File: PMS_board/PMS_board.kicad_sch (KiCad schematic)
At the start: 0 parts

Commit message: Added a Battery Managment chip
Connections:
- no-connect marks 0 -> 15
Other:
- added sheet Battery Management (BatteryManagement.kicad_sch)
- note added: "Temporarily put no connects to make ERC shut up"
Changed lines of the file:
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@@
 	(generator_version "10.0")
 	(paper "A4")
+	(text "Temporarily put no connects \nto make ERC shut up"
+		(exclude_from_sim no)
+		(at 88.646 48.006 0)
+		(effects
+			(font
+				(size 1.27 1.27)
+			)
+		)
+	)
+	(no_connect
+		(at 40.64 59.69)
+	)
+	(no_connect
+		(at 40.64 63.5)
+	)
+	(no_connect
+		(at 40.64 67.31)
+	)
+	(no_connect
+		(at 73.66 55.88)
+	)
+	(no_connect
+		(at 73.66 60.96)
+	)
+	(no_connect
+		(at 73.66 50.8)
+	)
+	(no_connect
+		(at 40.64 46.99)
+	)
+	(no_connect
+		(at 73.66 63.5)
+	)
+	(no_connect
+		(at 40.64 52.07)
+	)
+	(no_connect
+		(at 73.66 40.64)
+	)
+	(no_connect
+		(at 40.64 55.88)
+	)
+	(no_connect
+		(at 40.64 72.39)
+	)
+	(no_connect
+		(at 73.66 53.34)
+	)
+	(no_connect
+		(at 73.66 58.42)
+	)
+	(no_connect
+		(at 73.66 72.39)
+	)
+	(sheet
+		(at 40.64 35.56)
+		(size 33.02 41.91)
+		(exclude_from_sim no)
+		(in_bom yes)
+		(on_board yes)
+		(dnp no)
+		(fields_autoplaced yes)
+		(stroke
+			(width 0.1524)
+			(type solid)
+		)
+		(fill
+			(color 0 0 0 0)
+		)
+		(property "Sheetname" "Battery Management"
+			(at 40.64 34.8484 0)
+			(show_name no)
+			(do_not_autoplace no)
+			(effects
+				(font
+					(size 1.27 1.27)
+				)
+				(justify left bottom)
+			)
+		)
+		(property "Sheetfile" "BatteryManagement.kicad_sch"
+			(at 40.64 78.0546 0)
+			(show_name no)
+			(do_not_autoplace no)
+			(effects
+				(font
+					(size 1.27 1.27)
+				)
+				(justify left top)
+			)
+		)
+		(pin "1S" input
+			(at 40.64 67.31 180)
+			(effects
+				(font
+					(size 1.27 1.27)
+				)
+				(justify left)
+			)
+		)
+		(pin "2S" input
+			(at 40.64 63.5 180)
+			(effects
+				(font
+					(size 1.27 1.27)
+				)
+				(justify left)
+			)
+		)
+		(pin "3S" input
+			(at 40.64 59.69 180)
+			(effects
+				(font
+					(size 1.27 1.27)
+				)
+				(justify left)
+			)
+		)
+		(pin "4S" input
+			(at 40.64 55.88 180)
+			(effects
+				(font
+					(size 1.27 1.27)
+				)
+				(justify left)
+			)
+		)
+		(pin "5S" input
+			(at 40.64 52.07 180)
+			(effects
+				(font
+					(size 1.27 1.27)
+				)
+				(justify left)
+			)
+		)
+		(pin "FAULT" output
+			(at 73.66 50.8 0)
+			(effects
+				(font
+					(size 1.27 1.27)
+				)
+				(justify right)
+			)
+		)
+		(pin "MCU_RESET" input
+			(at 73.66 53.34 0)
+			(effects
+				(font
+					(size 1.27 1.27)
+				)
+				(justify right)
+			)
+		)
+		(pin "PACK+" input
+			(at 40.64 46.99 180)
+			(effects
+				(font
+					(size 1.27 1.27)
+				)
+				(justify left)
+			)
+		)
+		(pin "PACK-" input
+			(at 40.64 72.39 180)
+			(effects
+				(font
+					(size 1.27 1.27)
+				)
+				(justify left)
+			)
+		)
+		(pin "RDY" output
+			(at 73.66 55.88 0)
+			(effects
+				(font
+					(size 1.27 1.27)
+				)
+				(justify right)
+			)
+		)
+		(pin "SCL" bidirectional
+			(at 73.66 58.42 0)
+			(effects
+				(font
+					(size 1.27 1.27)
+				)
+				(justify right)
+			)
+		)
+		(pin "SDA" bidirectional
+			(at 73.66 60.96 0)
+			(effects
+				(font
+					(size 1.27 1.27)
+				)
+				(justify right)
+			)
+		)
+		(pin "WAKEUP" input
+			(at 73.66 63.5 0)
+			(effects
+				(font
+					(size 1.27 1.27)
+				)
+				(justify right)
+			)
+		)
+		(pin "VSC" output
+			(at 73.66 40.64 0)
+			(effects
+				(font
+					(size 1.27 1.27)
+				)
+				(justify right)
+			)
+		)
+		(pin "VSD" output
+			(at 73.66 72.39 0)
+			(effects
+				(font
+					(size 1.27 1.27)
+				)
+				(justify right)
+			)
+		)
+		(instances
+			(project "PMS_board"
+				(path "/282246b0-e0d8-4997-b3ee-58bf10355d52"
+					(page "2")
+				)
+			)
+		)
+	)
 	(sheet_instances
 		(path "/"

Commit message: add prep for hotswap
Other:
- added sheet HotSwap (hotswap.kicad_sch)
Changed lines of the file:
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@@
+		)
+	)
+	(sheet
+		(at 134.62 27.94)
+		(size 38.1 40.64)
+		(exclude_from_sim no)
+		(in_bom yes)
+		(on_board yes)
+		(dnp no)
+		(fields_autoplaced yes)
+		(stroke
+			(width 0.1524)
+			(type solid)
+		)
+		(fill
+			(color 0 0 0 0)
+		)
+		(property "Sheetname" "HotSwap"
+			(at 134.62 27.2284 0)
+			(show_name no)
+			(do_not_autoplace no)
+			(effects
+				(font
+					(size 1.27 1.27)
+				)
+				(justify left bottom)
+			)
+		)
+		(property "Sheetfile" "hotswap.kicad_sch"
+			(at 134.62 69.1646 0)
+			(show_name no)
+			(do_not_autoplace no)
+			(effects
+				(font
+					(size 1.27 1.27)
+				)
+				(justify left top)
+			)
+		)
+		(instances
+			(project "PMS_board"
+				(path "/282246b0-e0d8-4997-b3ee-58bf10355d52"
+					(page "3")
+				)
+			)
 		)
 	)

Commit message: Restored to stable commit
Idk wtf i'm doing
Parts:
- added D6: 1N5359B, Diode_THT:D_DO-201_P15.24mm_Horizontal, symbol Diode:1N53xxB
- added K1: AZSR190, Relay_THT:Relay_SPST-NO_Fujitsu_FTR-LYAA005x_FormA_Vertical, symbol Relay:Relay_SPST-NO
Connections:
- new net +24V: K1.14
- new net ESTOP: D6.1 (K), K1.A1
- new net PACK+: K1.13
- new net PACK-: D6.2 (A), K1.A2
- no-connect marks 15 -> 0
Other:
- removed sheet Battery Management
- added sheet Voltage Sensing (VoltageSensing.kicad_sch)
- note removed: "Temporarily put no connects to make ERC shut up"

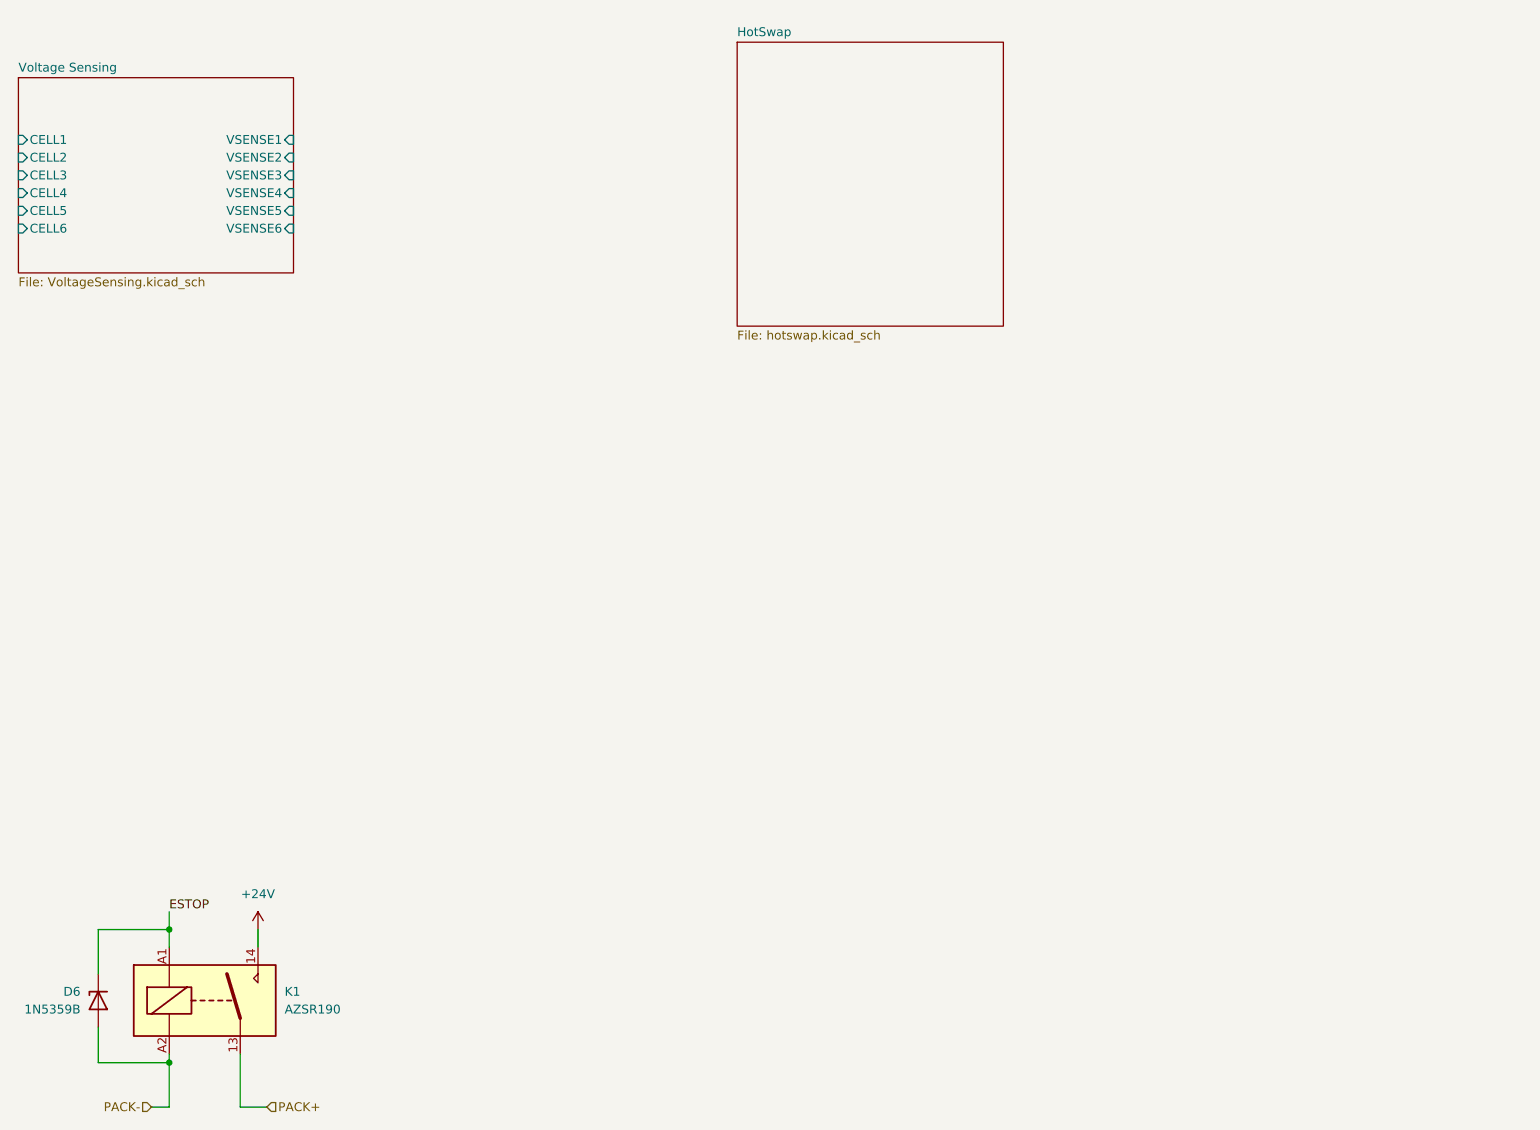
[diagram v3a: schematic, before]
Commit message: Added extra sheets
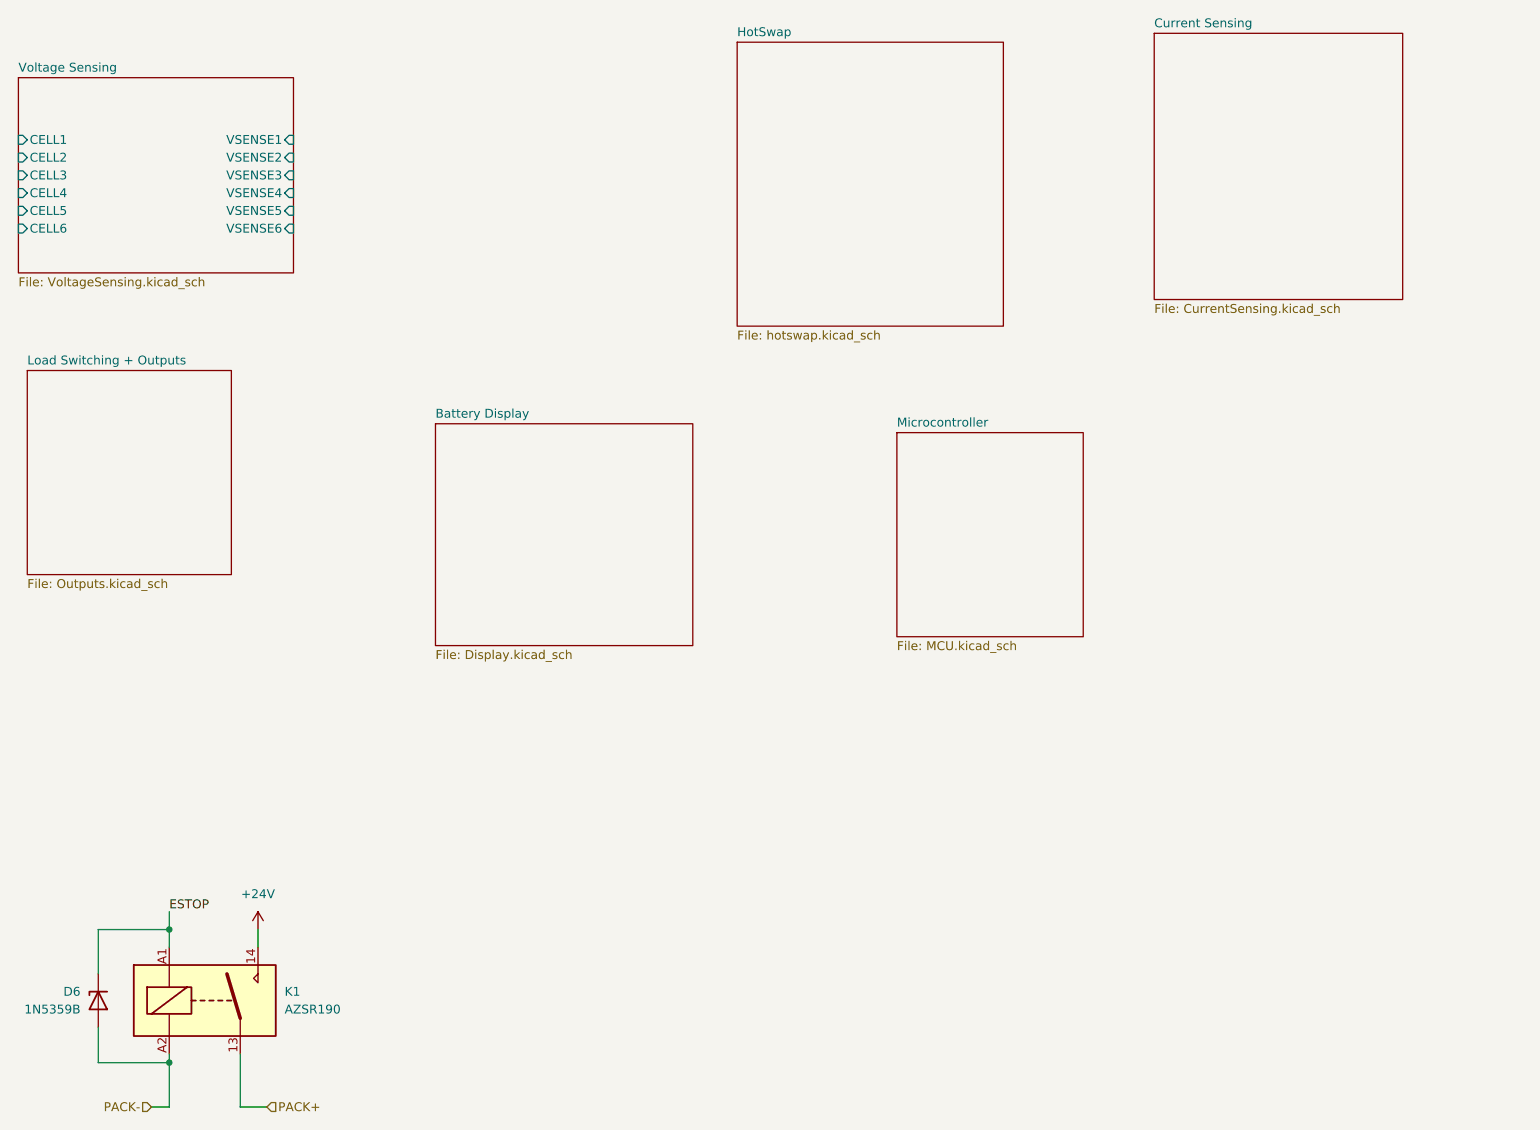
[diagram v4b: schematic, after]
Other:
- added sheet Battery Display (Display.kicad_sch)
- added sheet Current Sensing (CurrentSensing.kicad_sch)
- added sheet Load Switching + Outputs (Outputs.kicad_sch)
- added sheet Microcontroller (MCU.kicad_sch)
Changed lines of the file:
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@@
+	)
+	(sheet
+		(at 33.02 74.93)
+		(size 29.21 29.21)
+		(exclude_from_sim no)
+		(in_bom yes)
+		(on_board yes)
+		(dnp no)
+		(fields_autoplaced yes)
+		(stroke
+			(width 0.1524)
+			(type solid)
+		)
+		(fill
+			(color 0 0 0 0)
+		)
+		(property "Sheetname" "Load Switching + Outputs"
+			(at 33.02 74.2184 0)
+			(show_name no)
+			(do_not_autoplace no)
+			(effects
+				(font
+					(size 1.27 1.27)
+				)
+				(justify left bottom)
+			)
+		)
+		(property "Sheetfile" "Outputs.kicad_sch"
+			(at 33.02 104.7246 0)
+			(show_name no)
+			(do_not_autoplace no)
+			(effects
+				(font
+					(size 1.27 1.27)
+				)
+				(justify left top)
+			)
+		)
+		(instances
+			(project "PMS_board"
+				(path "/282246b0-e0d8-4997-b3ee-58bf10355d52"
+					(page "4")
+				)
+			)
+		)
+	)
+	(sheet
+		(at 157.48 83.82)
+		(size 26.67 29.21)
+		(exclude_from_sim no)
+		(in_bom yes)
+		(on_board yes)
+		(dnp no)
+		(fields_autoplaced yes)
+		(stroke
+			(width 0.1524)
+			(type solid)
+		)
+		(fill
+			(color 0 0 0 0)
+		)
+		(property "Sheetname" "Microcontroller"
+			(at 157.48 83.1084 0)
+			(show_name no)
+			(do_not_autoplace no)
+			(effects
+				(font
+					(size 1.27 1.27)
+				)
+				(justify left bottom)
+			)
+		)
+		(property "Sheetfile" "MCU.kicad_sch"
+			(at 157.48 113.6146 0)
+			(show_name no)
+			(do_not_autoplace no)
+			(effects
+				(font
+					(size 1.27 1.27)
+				)
+				(justify left top)
+			)
+		)
+		(instances
+			(project "PMS_board"
+				(path "/282246b0-e0d8-4997-b3ee-58bf10355d52"
+					(page "7")
+				)
+			)
+		)
+	)
+	(sheet
+		(at 91.44 82.55)
+		(size 36.83 31.75)
+		(exclude_from_sim no)
+		(in_bom yes)
+		(on_board yes)
+		(dnp no)
+		(fields_autoplaced yes)
+		(stroke
+			(width 0.1524)
+			(type solid)
+		)
+		(fill
+			(color 0 0 0 0)
+		)
+		(property "Sheetname" "Battery Display"
+			(at 91.44 81.8384 0)
+			(show_name no)
+			(do_not_autoplace no)
+			(effects
+				(font
+					(size 1.27 1.27)
+				)
+				(justify left bottom)
+			)
+		)
+		(property "Sheetfile" "Display.kicad_sch"
+			(at 91.44 114.8846 0)
+			(show_name no)
+			(do_not_autoplace no)
+			(effects
+				(font
+					(size 1.27 1.27)
+				)
+				(justify left top)
+			)
+		)
+		(instances
+			(project "PMS_board"
+				(path "/282246b0-e0d8-4997-b3ee-58bf10355d52"
+					(page "5")
+				)
+			)
+		)
 	)
 	(sheet
@@
 				)
 			)
+		)
+	)
+	(sheet
+		(at 194.31 26.67)
+		(size 35.56 38.1)
+		(exclude_from_sim no)
+		(in_bom yes)
+		(on_board yes)
+		(dnp no)
+		(fields_autoplaced yes)
+		(stroke
+			(width 0.1524)
+			(type solid)
+		)
+		(fill
+			(color 0 0 0 0)
+		)
+		(property "Sheetname" "Current Sensing"
+			(at 194.31 25.9584 0)
+			(show_name no)
+			(do_not_autoplace no)
+			(effects
+				(font
+					(size 1.27 1.27)
+				)
+				(justify left bottom)
+			)
+		)
+		(property "Sheetfile" "CurrentSensing.kicad_sch"
+			(at 194.31 65.3546 0)
+			(show_name no)
+			(do_not_autoplace no)
+			(effects
+				(font
+					(size 1.27 1.27)
+				)
+				(justify left top)
+			)
+		)
+		(instances
+			(project "PMS_board"
+				(path "/282246b0-e0d8-4997-b3ee-58bf10355d52"
+					(page "6")
+				)
+			)

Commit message: Forgot one lmao
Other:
- added sheet Power Smoothing + Conversion (SmoothingConversion.kicad_sch)
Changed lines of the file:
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@@
+		)
+	)
+	(sheet
+		(at 204.47 82.55)
+		(size 39.37 33.02)
+		(exclude_from_sim no)
+		(in_bom yes)
+		(on_board yes)
+		(dnp no)
+		(fields_autoplaced yes)
+		(stroke
+			(width 0.1524)
+			(type solid)
+		)
+		(fill
+			(color 0 0 0 0)
+		)
+		(property "Sheetname" "Power Smoothing + Conversion"
+			(at 204.47 81.8384 0)
+			(show_name no)
+			(do_not_autoplace no)
+			(effects
+				(font
+					(size 1.27 1.27)
+				)
+				(justify left bottom)
+			)
+		)
+		(property "Sheetfile" "SmoothingConversion.kicad_sch"
+			(at 204.47 116.1546 0)
+			(show_name no)
+			(do_not_autoplace no)
+			(effects
+				(font
+					(size 1.27 1.27)
+				)
+				(justify left top)
+			)
+		)
+		(instances
+			(project "PMS_board"
+				(path "/282246b0-e0d8-4997-b3ee-58bf10355d52"
+					(page "8")
+				)
+			)
 		)
 	)

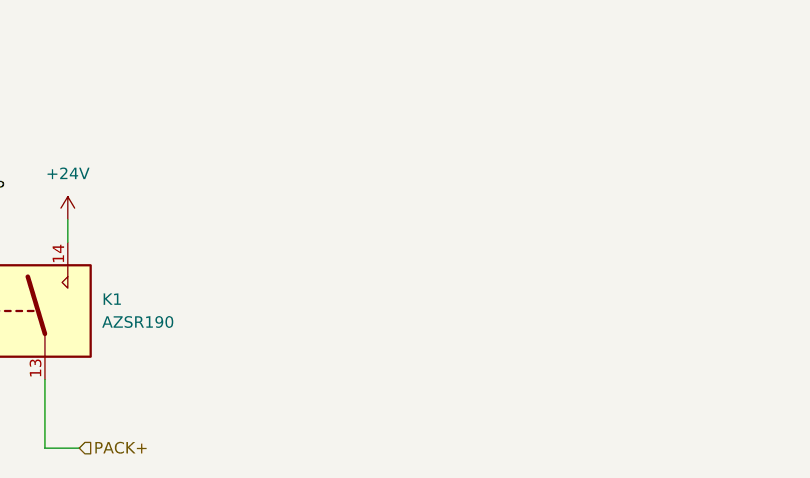
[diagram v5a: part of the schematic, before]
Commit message: Added switching circuit for each power rail
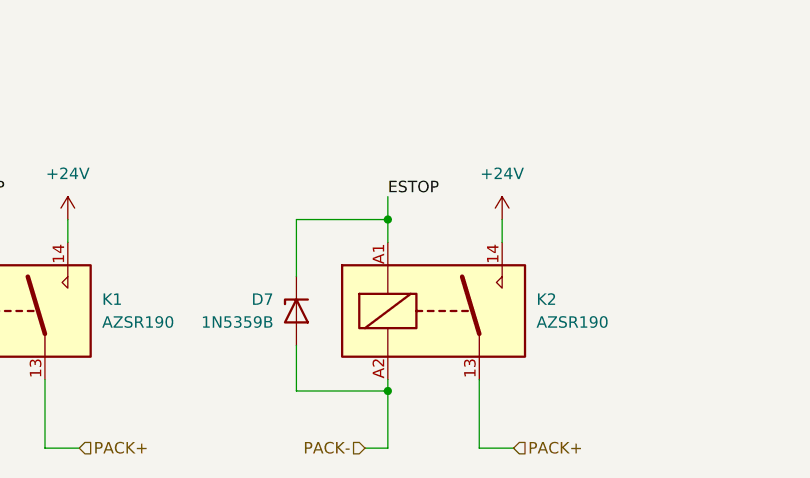
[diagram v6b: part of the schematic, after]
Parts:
- added D7: 1N5359B, Diode_THT:D_DO-201_P15.24mm_Horizontal, symbol Diode:1N53xxB
- added K2: AZSR190, Relay_THT:Relay_SPST-NO_Fujitsu_FTR-LYAA005x_FormA_Vertical, symbol Relay:Relay_SPST-NO
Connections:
- net +24V: now also K2.14
- net ESTOP: now also D7.1 (K), K2.A1
- net PACK+: now also K2.13
- net PACK-: now also D7.2 (A), K2.A2
